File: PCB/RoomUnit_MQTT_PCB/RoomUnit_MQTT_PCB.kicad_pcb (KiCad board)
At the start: 2 copper layers, 34.3 x 60 mm, 33 parts, among them J1 Conn_01x07_Socket, J2 Conn_01x07_Socket, Q1 MMBTA06, U1 LMV393, U2 TLV61046ADB

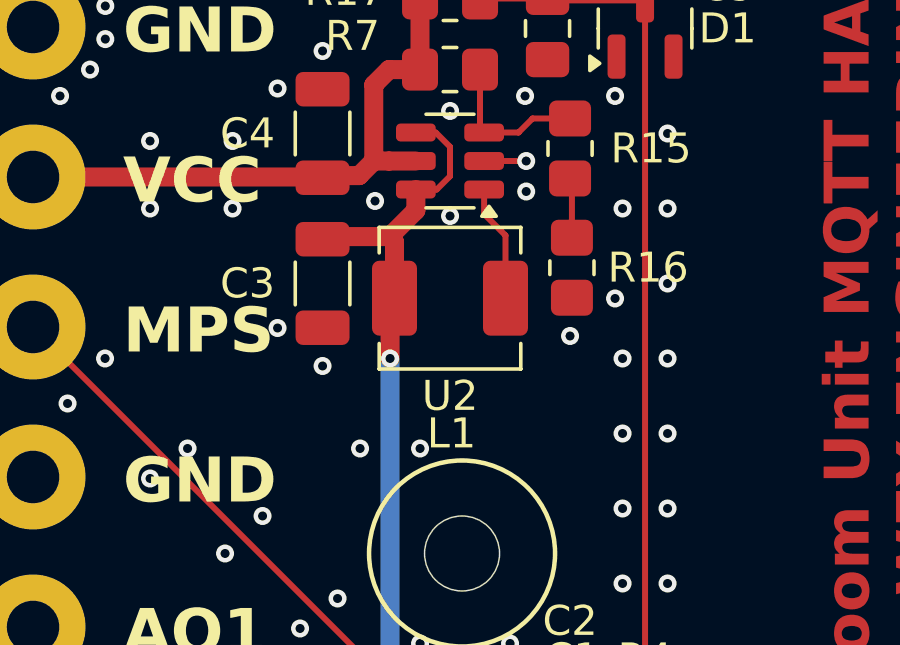
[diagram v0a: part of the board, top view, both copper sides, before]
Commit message: fixed placement and package
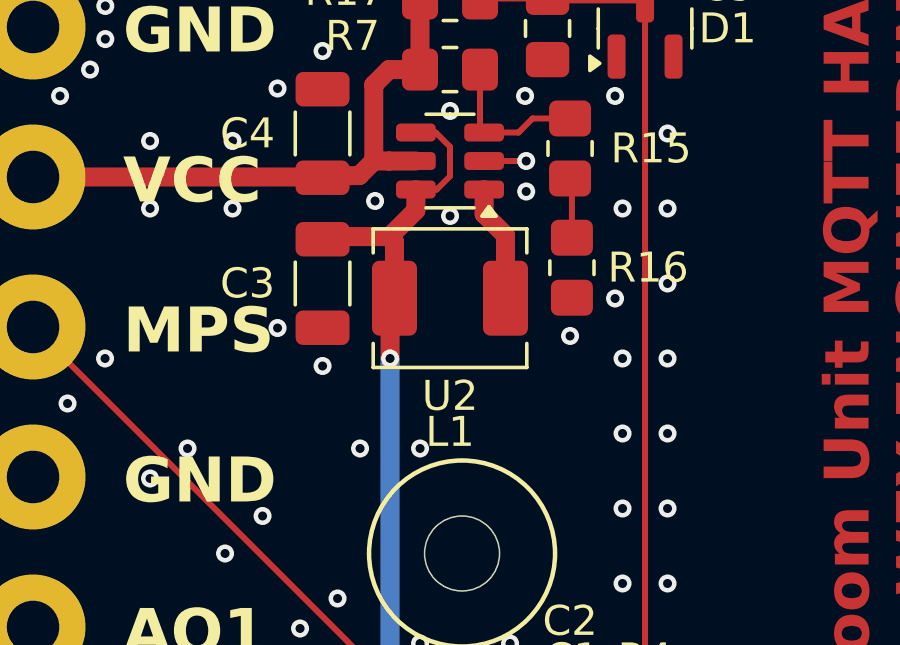
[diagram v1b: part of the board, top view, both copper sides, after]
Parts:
- L1: footprint Inductor_SMD:L_APV_APH0420 -> Inductor_SMD:L_Chilisin_BMRA00040420
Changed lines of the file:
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@@
 			)
 		)
+		(property "LCSC" "C17414"
+			(at 0 0 0)
+			(layer "F.SilkS")
+			(hide yes)
+			(effects
+				(font
+					(size 1.27 1.27)
+					(thickness 0.15)
+				)
+			)
+		)
 		(property ki_fp_filters "R_*")
 		(sheetname "/")
@@
 		(sheetname "/")
 		(sheetfile "RoomUnit_MQTT_PCB.kicad_sch")
-		(attr through_hole)
+		(attr through_hole exclude_from_bom)
 		(fp_text user "${REFERENCE}"
 			(at 1.2 -3.844 180)
@@
 			)
 		)
+		(property "LCSC" "C17414"
+			(at 0 0 0)
+			(layer "F.SilkS")
+			(hide yes)
+			(effects
+				(font
+					(size 1.27 1.27)
+					(thickness 0.15)
+				)
+			)
+		)
 		(property ki_fp_filters "R_*")
 		(sheetname "/")
 		(sheetfile "RoomUnit_MQTT_PCB.kicad_sch")
-		(attr smd)
+		(attr smd exclude_from_bom)
 		(fp_line
 			(start -0.227064 -0.735)
@@
 			)
 		)
+		(property "LCSC" "C17414"
+			(at 0 0 0)
+			(layer "F.SilkS")
+			(hide yes)
+			(effects
+				(font
+					(size 1.27 1.27)
+					(thickness 0.15)
+				)
+			)
+		)
 		(property ki_fp_filters "R_*")
 		(sheetname "/")
@@
 		(sheetname "/")
 		(sheetfile "RoomUnit_MQTT_PCB.kicad_sch")
-		(attr through_hole)
+		(attr through_hole exclude_from_bom)
 		(fp_text user "${REFERENCE}"
 			(at -1 -3.344 180)
@@
 			)
 		)
+		(property "LCSC" "C17414"
+			(at 0 0 0)
+			(layer "F.SilkS")
+			(hide yes)
+			(effects
+				(font
+					(size 1.27 1.27)
+					(thickness 0.15)
+				)
+			)
+		)
 		(property ki_fp_filters "R_*")
 		(sheetname "/")
 		(sheetfile "RoomUnit_MQTT_PCB.kicad_sch")
-		(attr smd)
+		(attr smd exclude_from_bom)
 		(fp_line
 			(start -0.227064 -0.735)
@@
 		)
 	)
-	(footprint "Inductor_SMD:L_APV_APH0420"
+	(footprint "Inductor_SMD:L_Chilisin_BMRA00040420"
 		(layer "F.Cu")
 		(at 166.248 51.74)
-		(descr "Inductor, APV, APH0420, 4.2x4.2x1.8mm, (http://en.apvind.com/public/upload/20240408/996aafa961154ed753e4983e7eb80fa7.pdf), generated with kicad-footprint-generator gen_inductor.py")
-		(tags "Inductor molded power shielded")
+		(descr "Inductor, Chilisin, BMRA00040420, 4.6x4.1x2.0mm, (https://www.chilisin.com/upload/media/product/power/file/BMRx_Series.pdf), generated with kicad-footprint-generator gen_inductor.py")
+		(tags "Inductor bmrx mchi")
 		(property "Reference" "L1"
-			(at 0.0508 4.51 180)
+			(at 0 4.46 0)
 			(layer "F.SilkS")
 			(effects
@@
 		)
 		(property "Value" "10u"
-			(at 0 3.1 0)
+			(at 0 3.05 0)
 			(layer "F.Fab")
 			(effects
@@
 			)
 		)
-		(property "LCSC" "C1329533"
+		(property "LCSC" "C133195"
 			(at 0 0 0)
 			(layer "F.SilkS")
@@
 		(attr smd)
 		(fp_line
-			(start -2.36 -2.36)
-			(end -2.36 -1.51)
+			(start -2.56 -2.31)
+			(end -2.56 -1.51)
 			(stroke
 				(width 0.12)
@@
 		)
 		(fp_line
-			(start -2.36 -2.36)
-			(end 2.36 -2.36)
+			(start -2.56 -2.31)
+			(end 2.56 -2.31)
 			(stroke
 				(width 0.12)
@@
 		)
 		(fp_line
-			(start -2.36 2.36)
-			(end -2.36 1.51)
+			(start -2.56 2.31)
+			(end -2.56 1.51)
 			(stroke
 				(width 0.12)
@@
 		)
 		(fp_line
-			(start -2.36 2.36)
-			(end 2.36 2.36)
+			(start -2.56 2.31)
+			(end 2.56 2.31)
 			(stroke
 				(width 0.12)
@@
 		)
 		(fp_line
-			(start 2.36 -2.36)
-			(end 2.36 -1.51)
+			(start 2.56 -2.31)
+			(end 2.56 -1.51)
 			(stroke
 				(width 0.12)
@@
 		)
 		(fp_line
-			(start 2.36 2.36)
-			(end 2.36 1.51)
+			(start 2.56 2.31)
+			(end 2.56 1.51)
 			(stroke
 				(width 0.12)
@@
 		)
 		(fp_line
-			(start -2.85 -2.35)
-			(end -2.85 2.35)
+			(start -2.85 -2.3)
+			(end -2.85 2.3)
 			(stroke
 				(width 0.05)
@@
 		)
 		(fp_line
-			(start -2.85 2.35)
-			(end 2.85 2.35)
+			(start -2.85 2.3)
+			(end 2.85 2.3)
 			(stroke
 				(width 0.05)
@@
 		)
 		(fp_line
-			(start 2.85 -2.35)
-			(end -2.85 -2.35)
+			(start 2.85 -2.3)
+			(end -2.85 -2.3)
 			(stroke
 				(width 0.05)
@@
 		)
 		(fp_line
-			(start 2.85 2.35)
-			(end 2.85 -2.35)
+			(start 2.85 2.3)
+			(end 2.85 -2.3)
 			(stroke
 				(width 0.05)
@@
 		)
 		(fp_line
-			(start -2.1 -2.1)
-			(end -2.1 2.1)
+			(start -2.3 -2.05)
+			(end -2.3 2.05)
 			(stroke
 				(width 0.1)
@@
 		)
 		(fp_line
-			(start -2.1 2.1)
-			(end 2.1 2.1)
+			(start -2.3 2.05)
+			(end 2.3 2.05)
 			(stroke
 				(width 0.1)
@@
 		)
 		(fp_line
-			(start 2.1 -2.1)
-			(end -2.1 -2.1)
+			(start 2.3 -2.05)
+			(end -2.3 -2.05)
 			(stroke
 				(width 0.1)
@@
 		)
 		(fp_line
-			(start 2.1 2.1)
-			(end 2.1 -2.1)
+			(start 2.3 2.05)
+			(end 2.3 -2.05)
 			(stroke
 				(width 0.1)
@@
 		)
 		(embedded_fonts no)
-		(model "${KICAD8_3DMODEL_DIR}/Inductor_SMD.3dshapes/L_APV_APH0420.wrl"
+		(model "${KICAD9_3DMODEL_DIR}/Inductor_SMD.3dshapes/L_Chilisin_BMRA00040420.wrl"
 			(offset
 				(xyz 0 0 0)
@@
 			)
 		)
+		(property "LCSC" "C17414"
+			(at 0 0 0)
+			(layer "F.SilkS")
+			(hide yes)
+			(effects
+				(font
+					(size 1.27 1.27)
+					(thickness 0.15)
+				)
+			)
+		)
 		(property ki_fp_filters "R_*")
 		(sheetname "/")
 		(sheetfile "RoomUnit_MQTT_PCB.kicad_sch")
-		(attr smd)
+		(attr smd exclude_from_bom)
 		(fp_line
 			(start -0.227064 -0.735)
@@
 		(sheetname "/")
 		(sheetfile "RoomUnit_MQTT_PCB.kicad_sch")
-		(attr through_hole)
+		(attr through_hole exclude_from_bom)
 		(fp_text user "MPS"
 			(at 3 11 0)
@@
 			)
 		)
+		(property "LCSC" "C17414"
+			(at 0 0 0)
+			(layer "F.SilkS")
+			(hide yes)
+			(effects
+				(font
+					(size 1.27 1.27)
+					(thickness 0.15)
+				)
+			)
+		)
 		(property ki_fp_filters "R_*")
 		(sheetname "/")
@@
 			)
 		)
-		(property "LCSC" "C544665"
+		(property "LCSC" "C7984"
 			(at 0 0 0)
 			(layer "F.SilkS")
@@
 			(keep_text_aligned yes)
 		)
-		(gr_text "60.0000 mm"
+		(gr_text "2362.2047 mils"
 			(at 146.2 70 90)
 			(layer "F.Cu")
@@
 			(keep_text_aligned yes)
 		)
-		(gr_text "18.3 mm"
+		(gr_text "720.5 mils"
 			(at 167 107 0)
 			(layer "F.Cu")
@@
 			(keep_text_aligned yes)
 		)
-		(gr_text "8.0 mm"
+		(gr_text "315.0 mils"
 			(at 154 107 0)
 			(layer "F.Cu")
@@
 			(keep_text_aligned yes)
 		)
-		(gr_text "34.3000 mm"
+		(gr_text "1350.3937 mils"
 			(at 167.15 36.7 0)
 			(layer "F.Cu")
@@
 			(keep_text_aligned yes)
 		)
-		(gr_text "8.0 mm"
+		(gr_text "313.0 mils"
 			(at 180.473743 107 0)
 			(layer "F.Cu")
@@
 	)
 	(segment
-		(start 168.098 51.74)
-		(end 168.098 49.6475)
-		(width 0.2)
+		(start 168.098 49.6475)
+		(end 167.3855 48.935)
+		(width 0.635)
 		(layer "F.Cu")
 		(net 15)
 	)
 	(segment
-		(start 167.3855 48.935)
-		(end 167.3855 48.118)
-		(width 0.2)
+		(start 168.098 51.74)
+		(end 168.098 49.6475)
+		(width 0.635)
 		(layer "F.Cu")
 		(net 15)
 	)
 	(segment
-		(start 168.098 49.6475)
-		(end 167.3855 48.935)
-		(width 0.2)
+		(start 167.3855 48.935)
+		(end 167.3855 48.118)
+		(width 0.635)
 		(layer "F.Cu")
 		(net 15)
